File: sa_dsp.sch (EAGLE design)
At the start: 327 parts, among them CN1 uSD, CN3 2X5 HEADER, Q3 2N7002, Q4 2N7002, SW1 1825910-7, U1 PGA2311, U10 LME49720, U11 PGA2311, U12 LME49720, U13 LME49720, U14 PCM1754, U15 LME49720, U16 PGA2311, U17 LME49720, U18 LME49720, U19 PCM1754, U2 LM317, U20 LME49720, U21 7 SEG, U22 74HC164A, U23 PCM2707, U24 PCM2707, U25 7 SEG, U26 74HC164A, U27 LM337, U28 LM317, U29 7 SEG, U3 OSD3358-512M-BSM, U30 74HC164A, U31 100MHz, U4 LME49720, U5 LME49720, U6 10CL016YF484C6G, U7 7 SEG, U8 74HC164A, U9 PCM1754

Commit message: DSP progress
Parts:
- added C133: 2.2uF 25V, CAPACITORS:GRM188R61E225KA12D
- added C134, C138: 100pF 50V, CAPACITORS:C0603C101K5GACTU
- added C135, C136, C137, C139: 100nF 16V, CAPACITORS:CL10B104KO8WPNC
- added CN2, CN4: MINI B USB, CONNECTORs:MUSB-05-S-B-SM-A
- added FB17, FB6: 600R, INDUCTORS:742792651
- added TP3, TP4, TP5, TP6, TP7: 2MM_TEST_POINT, MISC:2MM_TEST_POINT
- added U32, U34: USBLC6-2SC6, ICs:USBLC6-2SC6
- added U33: FT230X, ICs:FT230XS
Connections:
- removed net AM_STM_NRST: U3C.GPMC_AD9
- removed net STM32_BOOT0: U3C.GPMC_AD10
- new net AM_I2C0_SCL: TP3.P$1, U3A.I2C0_SCL, U3A.PMIC_SCL
- new net AM_I2C0_SDA: TP4.P$1, U3A.I2C0_SDA, U3A.PMIC_SDA
- new net FT_DB_3V3: C133.2, C137.2, U33.!CTS, U33.!RESET, U33.3V3OUT, U33.VCCIO
- new net FT_DB_USB_5V: C134.2, C135.2, C136.2, FB6.2, U32.VBUS, U33.VCC
- new net N$183: CN2.D-, U32.D+_OUT
- new net N$199: CN2.D+, U32.D-OUT
- new net N$200: U32.D+_IN, U33.D-
- new net N$201: U32.D-_IN, U33.D+
- new net N$202: CN2.5V, FB6.1
- new net N$203: CN4.5V, FB17.1
- new net OSD_SPI_CS_FPGA: U3C.SPI0_CS0
- new net OSD_SPI_MISO: U3C.SPI0_D1
- new net OSD_SPI_MOSI: U3C.SPI0_D0
- new net OSD_SPI_SCLK: U3C.SPI0_SCLK
- net 5VUSB: now also C138.2, C139.2, FB17.2, U34.VBUS
- net AM_DEBUG_UART_RX: now also U33.RXD
- net AM_DEBUG_UART_TX: now also U33.TXD
- net AM_EEPROM_WP: now also TP5.P$1
- net AM_WARM_!RST: now also TP7.P$1
- net GND: now also C133.1, C134.1, C135.1, C136.1, C137.1, C138.1, C139.1, CN2.GND, CN4.GND, TP6.P$1, U32.GND, U33.GND, U34.GND
- net N$134: now also CN4.D-, U34.D-OUT; no longer U3A.I2C0_SCL, U3A.PMIC_SCL
- net N$135: now also CN4.D+, U34.D+_OUT; no longer U3A.I2C0_SDA, U3A.PMIC_SDA
- net N$172: now also R103.1, U34.D-_IN; no longer R102.1
- net N$173: now also R102.1, U34.D+_IN; no longer R103.1
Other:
- moved on the sheet: C119, C120, C121, C122, C123, C124, C125, C93, C94, C95, R102, R103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

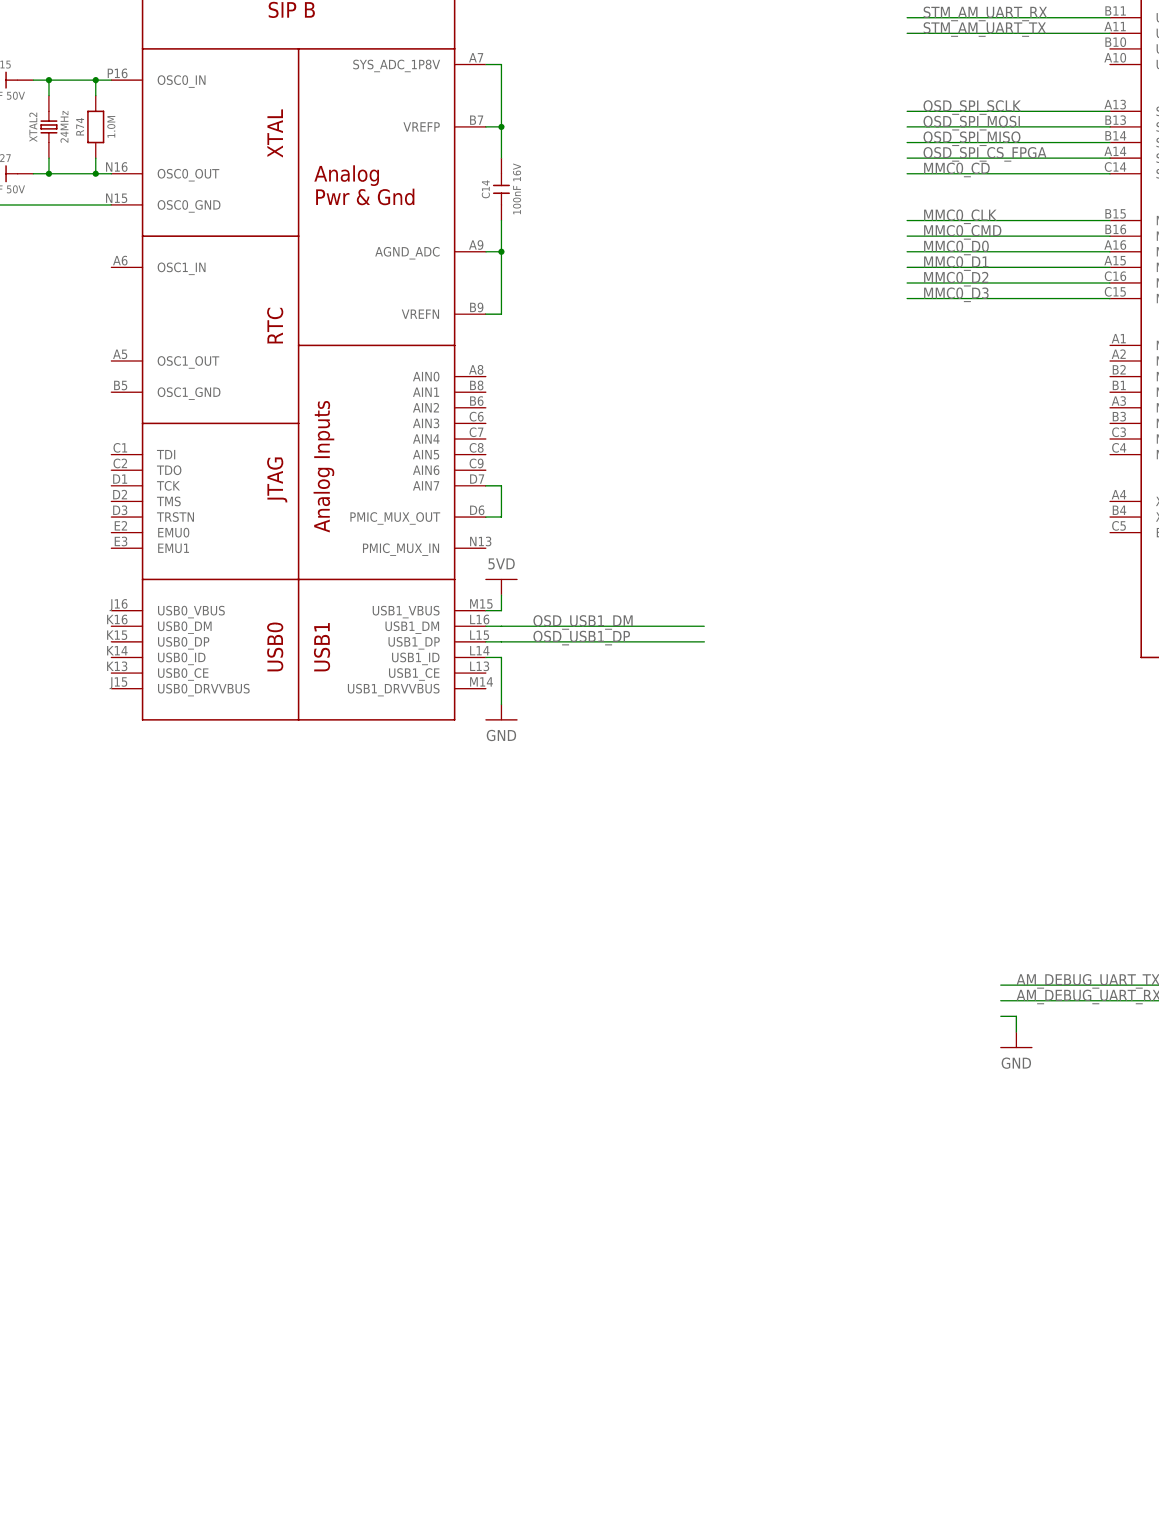
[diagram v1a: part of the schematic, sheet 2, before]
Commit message: Added female USB
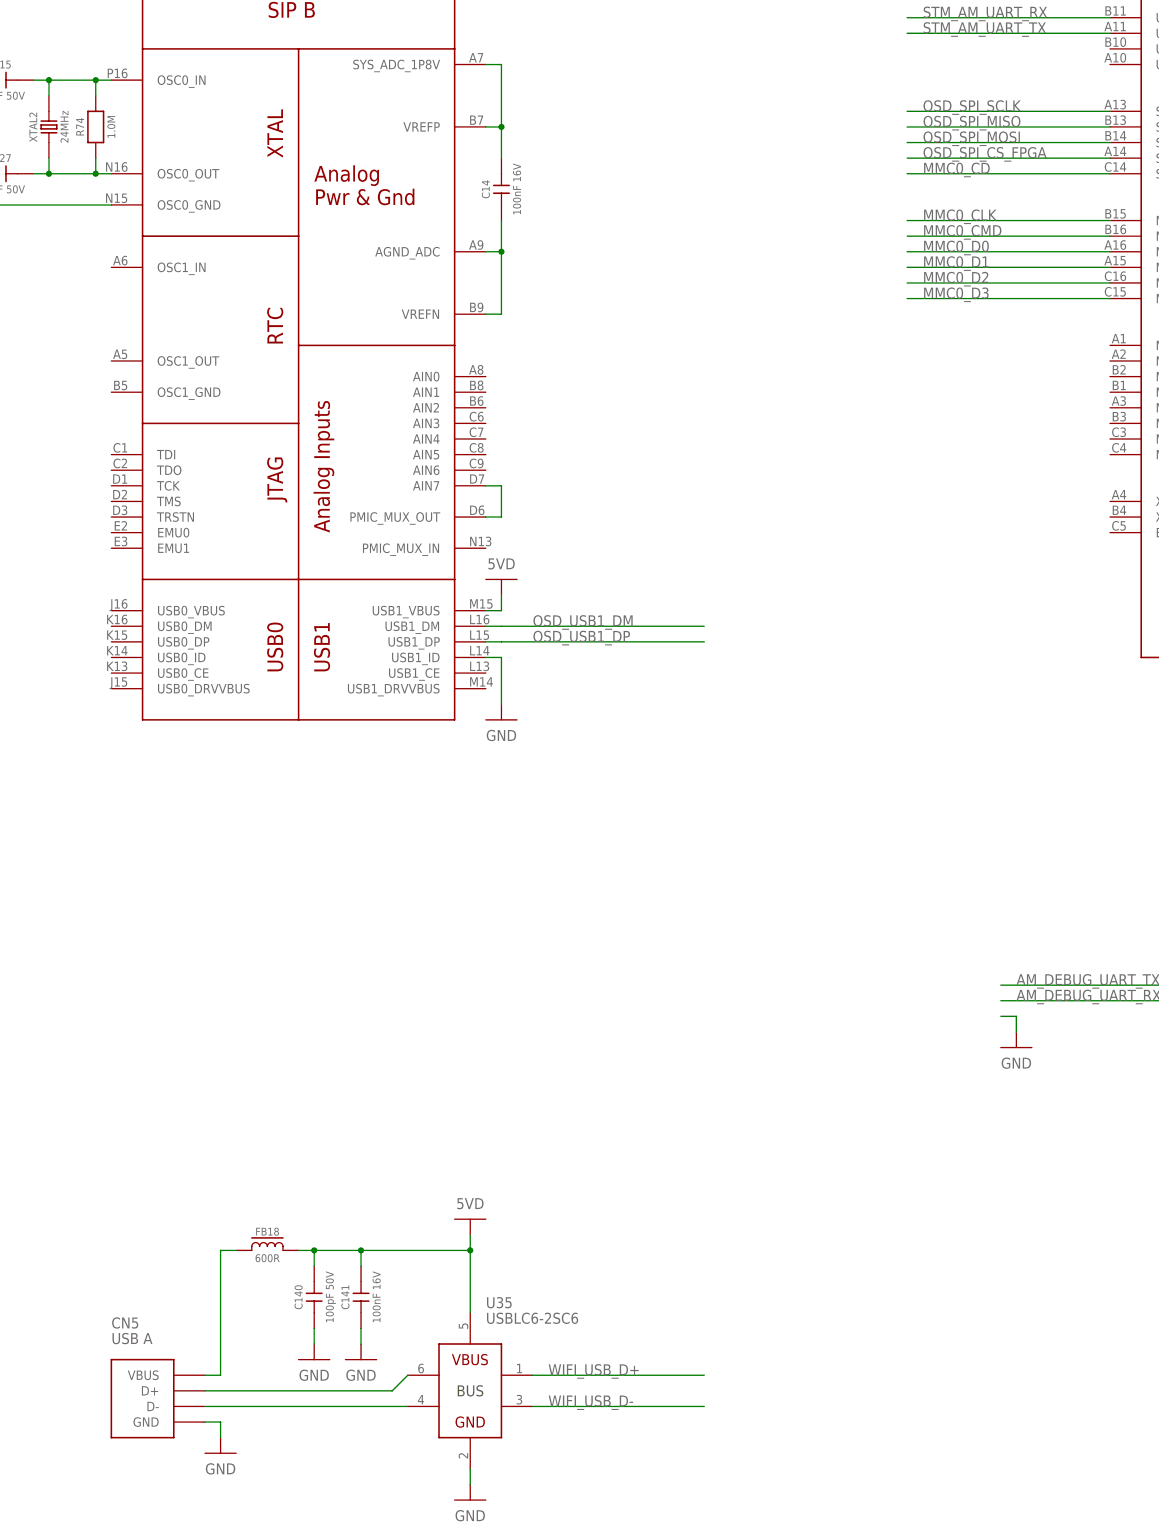
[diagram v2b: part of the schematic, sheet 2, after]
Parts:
- added C140: 100pF 50V, CAPACITORS:C0603C101K5GACTU
- added C141: 100nF 16V, CAPACITORS:CL10B104KO8WPNC
- added CN5: USB A, CONNECTORs:629104190121
- added FB18: 600R, INDUCTORS:742792651
- added U35: USBLC6-2SC6, ICs:USBLC6-2SC6
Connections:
- new net N$204: CN5.D-, U35.D-OUT
- new net N$205: CN5.D+, U35.D+_OUT
- new net N$206: CN5.VBUS, FB18.1
- new net WIFI_USB_D+: U35.D+_IN
- new net WIFI_USB_D-: U35.D-_IN
- net 5VD: now also C140.2, C141.2, FB18.2, U35.VBUS
- net GND: now also C140.1, C141.1, CN5.GND, U35.GND
- net OSD_SPI_MISO: now also U3C.SPI0_D0; no longer U3C.SPI0_D1
- net OSD_SPI_MOSI: now also U3C.SPI0_D1; no longer U3C.SPI0_D0
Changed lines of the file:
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@@
 <part name="U$200" library="NETS" deviceset="5VUSB" device=""/>
 <part name="TP7" library="MISC" deviceset="2MM_TEST_POINT" device=""/>
+<part name="CN5" library="CONNECTORs" deviceset="629104190121" device="" value="USB A"/>
+<part name="U$201" library="NETS" deviceset="5VD" device=""/>
+<part name="U35" library="ICs" deviceset="USBLC6-2SC6" device="" value="USBLC6-2SC6"/>
+<part name="GND130" library="NETS" deviceset="GND" device=""/>
+<part name="FB18" library="INDUCTORS" deviceset="742792651" device="" value="600R"/>
+<part name="C140" library="CAPACITORS" deviceset="C0603C101K5GACTU" device="" value="100pF 50V"/>
+<part name="C141" library="CAPACITORS" deviceset="CL10B104KO8WPNC" device="" value="100nF 16V"/>
+<part name="GND131" library="NETS" deviceset="GND" device=""/>
+<part name="GND132" library="NETS" deviceset="GND" device=""/>
+<part name="GND133" library="NETS" deviceset="GND" device=""/>
 </parts>
 <sheets>
@@
 <attribute name="NAME" x="-68.58" y="132.08" size="1.27" layer="97" rot="R90" align="center"/>
 </instance>
+<instance part="CN5" gate="G$1" x="205.74" y="-2.54" smashed="yes">
+<attribute name="NAME" x="200.66" y="7.62" size="1.778" layer="95"/>
+<attribute name="VALUE" x="200.66" y="5.08" size="1.778" layer="96"/>
+</instance>
+<instance part="U$201" gate="G$1" x="259.08" y="25.4" smashed="yes">
+<attribute name="VALUE" x="259.08" y="27.94" size="1.778" layer="96" rot="R180" align="center"/>
+</instance>
+<instance part="U35" gate="G$1" x="259.08" y="-2.54" smashed="yes" rot="MR0">
+<attribute name="NAME" x="261.62" y="12.7" size="1.778" layer="95" rot="MR180"/>
+<attribute name="VALUE" x="261.62" y="10.16" size="1.778" layer="95" rot="MR180"/>
+</instance>
+<instance part="GND130" gate="G$1" x="259.08" y="-20.32" smashed="yes">
+<attribute name="VALUE" x="259.08" y="-22.86" size="1.778" layer="96" align="center"/>
+</instance>
+<instance part="FB18" gate="G$1" x="226.06" y="20.32" smashed="yes">
+<attribute name="NAME" x="226.06" y="23.368" size="1.27" layer="95" align="center"/>
+<attribute name="VALUE" x="226.06" y="19.05" size="1.27" layer="96" align="center"/>
+</instance>
+<instance part="C140" gate="G$1" x="233.68" y="12.7" smashed="yes" rot="R90">
+<attribute name="NAME" x="231.14" y="12.7" size="1.27" layer="95" rot="R90" align="center"/>
+<attribute name="VALUE" x="236.22" y="12.7" size="1.27" layer="96" rot="R90" align="center"/>
+</instance>
+<instance part="C141" gate="G$1" x="241.3" y="12.7" smashed="yes" rot="R90">
+<attribute name="NAME" x="238.76" y="12.7" size="1.27" layer="95" rot="R90" align="center"/>
+<attribute name="VALUE" x="243.84" y="12.7" size="1.27" layer="96" rot="R90" align="center"/>
+</instance>
+<instance part="GND131" gate="G$1" x="241.3" y="2.54" smashed="yes">
+<attribute name="VALUE" x="241.3" y="0" size="1.778" layer="96" align="center"/>
+</instance>
+<instance part="GND132" gate="G$1" x="233.68" y="2.54" smashed="yes">
+<attribute name="VALUE" x="233.68" y="0" size="1.778" layer="96" align="center"/>
+</instance>
+<instance part="GND133" gate="G$1" x="218.44" y="-12.7" smashed="yes">
+<attribute name="VALUE" x="218.44" y="-15.24" size="1.778" layer="96" align="center"/>
+</instance>
 </instances>
 <busses>
@@
 <wire x1="523.24" y1="490.22" x2="523.24" y2="487.68" width="0.1524" layer="91"/>
 </segment>
+<segment>
+<pinref part="U35" gate="G$1" pin="GND"/>
+<pinref part="GND130" gate="G$1" pin="GND"/>
+<wire x1="259.08" y1="-17.78" x2="259.08" y2="-15.24" width="0.1524" layer="91"/>
+</segment>
+<segment>
+<pinref part="C141" gate="G$1" pin="1"/>
+<pinref part="GND131" gate="G$1" pin="GND"/>
+<wire x1="241.3" y1="7.62" x2="241.3" y2="5.08" width="0.1524" layer="91"/>
+</segment>
+<segment>
+<pinref part="C140" gate="G$1" pin="1"/>
+<pinref part="GND132" gate="G$1" pin="GND"/>
+<wire x1="233.68" y1="7.62" x2="233.68" y2="5.08" width="0.1524" layer="91"/>
+</segment>
+<segment>
+<pinref part="CN5" gate="G$1" pin="GND"/>
+<wire x1="215.9" y1="-7.62" x2="218.44" y2="-7.62" width="0.1524" layer="91"/>
+<pinref part="GND133" gate="G$1" pin="GND"/>
+<wire x1="218.44" y1="-7.62" x2="218.44" y2="-10.16" width="0.1524" layer="91"/>
+</segment>
 </net>
 <net name="N$124" class="0">
@@
 <label x="370.84" y="449.58" size="1.778" layer="95"/>
 </segment>
+<segment>
+<pinref part="U35" gate="G$1" pin="VBUS"/>
+<wire x1="259.08" y1="10.16" x2="259.08" y2="20.32" width="0.1524" layer="91"/>
+<wire x1="231.14" y1="20.32" x2="233.68" y2="20.32" width="0.1524" layer="91"/>
+<pinref part="FB18" gate="G$1" pin="2"/>
+<pinref part="C140" gate="G$1" pin="2"/>
+<wire x1="233.68" y1="20.32" x2="241.3" y2="20.32" width="0.1524" layer="91"/>
+<wire x1="241.3" y1="20.32" x2="259.08" y2="20.32" width="0.1524" layer="91"/>
+<wire x1="233.68" y1="17.78" x2="233.68" y2="20.32" width="0.1524" layer="91"/>
+<junction x="233.68" y="20.32"/>
+<pinref part="C141" gate="G$1" pin="2"/>
+<wire x1="241.3" y1="17.78" x2="241.3" y2="20.32" width="0.1524" layer="91"/>
+<junction x="241.3" y="20.32"/>
+<pinref part="U$201" gate="G$1" pin="5VD"/>
+<wire x1="259.08" y1="22.86" x2="259.08" y2="20.32" width="0.1524" layer="91"/>
+<junction x="259.08" y="20.32"/>
+</segment>
 </net>
 <net name="N$183" class="0">
@@
 </segment>
 </net>
-<net name="OSD_SPI_MOSI" class="0">
+<net name="OSD_SPI_MISO" class="0">
 <segment>
 <pinref part="U3" gate="C" pin="SPI0_D0"/>
@@
 </segment>
 </net>
-<net name="OSD_SPI_MISO" class="0">
+<net name="OSD_SPI_MOSI" class="0">
 <segment>
 <pinref part="U3" gate="C" pin="SPI0_D1"/>
@@
 </segment>
 </net>
+<net name="N$204" class="0">
+<segment>
+<pinref part="U35" gate="G$1" pin="D-OUT"/>
+<pinref part="CN5" gate="G$1" pin="D-"/>
+<wire x1="248.92" y1="-5.08" x2="215.9" y2="-5.08" width="0.1524" layer="91"/>
+</segment>
+</net>
+<net name="N$205" class="0">
+<segment>
+<pinref part="CN5" gate="G$1" pin="D+"/>
+<pinref part="U35" gate="G$1" pin="D+_OUT"/>
+<wire x1="215.9" y1="-2.54" x2="246.38" y2="-2.54" width="0.1524" layer="91"/>
+<wire x1="246.38" y1="-2.54" x2="248.92" y2="0" width="0.1524" layer="91"/>
+</segment>
+</net>
+<net name="N$206" class="0">
+<segment>
+<pinref part="FB18" gate="G$1" pin="1"/>
+<wire x1="220.98" y1="20.32" x2="218.44" y2="20.32" width="0.1524" layer="91"/>
+<wire x1="218.44" y1="20.32" x2="218.44" y2="0" width="0.1524" layer="91"/>
+<pinref part="CN5" gate="G$1" pin="VBUS"/>
+<wire x1="218.44" y1="0" x2="215.9" y2="0" width="0.1524" layer="91"/>
+</segment>
+</net>
+<net name="WIFI_USB_D+" class="0">
+<segment>
+<pinref part="U35" gate="G$1" pin="D+_IN"/>
+<wire x1="269.24" y1="0" x2="297.18" y2="0" width="0.1524" layer="91"/>
+<label x="271.78" y="0" size="1.778" layer="95"/>
+</segment>
+</net>
+<net name="WIFI_USB_D-" class="0">
+<segment>
+<pinref part="U35" gate="G$1" pin="D-_IN"/>
+<wire x1="269.24" y1="-5.08" x2="297.18" y2="-5.08" width="0.1524" layer="91"/>
+<label x="271.78" y="-5.08" size="1.778" layer="95"/>
+</segment>
+</net>

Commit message: USB hub added
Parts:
- added C149, C150: 10pF 100V, CAPACITORS:06031A100FAT2A
- added C151, C152, C153, C154, C155: 100nF 16V, CAPACITORS:CL10B104KO8WPNC
- added CN6: MINI B USB, CONNECTORs:MUSB-05-S-B-SM-A
- added R133: 10k, r_0603:ERJ3EKF1002V
- added R134: 20k, r_0603:ERJ3EKF2002V
- added R135, R137, R138: 51k, r_0603:ERJ3EKF5102V
- added R136: 12k, r_0603:ERJ3EKF1202V
- added R139: 1.0M, r_0603:ERJ3EKF1004V
- added U36: USBLC6-2SC6, ICs:USBLC6-2SC6
- added U37: 2 PORT HUB, ICs:USB2412
- added XTAL5: 24MHz, CRYSTALS:7A-24.000MAAJ-T
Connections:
- removed net WIFI_USB_D+: U35.D+_IN
- removed net WIFI_USB_D-: U35.D-_IN
- new net N$207: U3B.USB1_DRVVBUS, U3B.USB1_VBUS
- new net N$208: CN6.D+, U36.D+_OUT
- new net N$209: CN6.D-, U36.D-OUT
- new net N$229: R133.2, R134.2, U37.VBUS_DECT
- new net N$230: R135.2, U37.HS_IND
- new net N$231: R136.2, U37.RBIAS
- new net N$232: R138.2, U37.NON_REM1
- new net N$233: R137.2, U37.SUSP_IND/NON_REM0
- new net N$234: C150.2, R139.2, U37.XTALIN/CLKLIN, XTAL5.P$1
- new net N$235: C149.2, R139.1, U37.XTALOUT, XTAL5.P$2
- new net OSD_DEBUG_USB_DM: U36.D-_IN, U3B.USB0_DM
- new net OSD_DEBUG_USB_DP: U36.D+_IN, U3B.USB0_DP
- new net OSD_DEBUG_USB_ID: CN6.ID, U3B.USB0_ID
- new net USB_OUT0_DN: U35.D-_IN, U37.USB_DN1_DN
- new net USB_OUT0_DP: U35.D+_IN, U37.USB_DN1_DP
- new net USB_OUT1_DN: R89.1, U37.USB_DN2_DN
- new net USB_OUT1_DP: R88.1, U37.USB_DN2_DP
- new net USB_RESET: U37.!RESET
- net 3V3: now also C151.2, C152.2, C153.2, C154.2, C155.2, U37.VDD
- net 5VD: now also U3B.USB0_VBUS; no longer U3B.USB1_VBUS
- net 5VUSB: now also R133.1
- net GND: now also C149.1, C150.1, C151.1, C152.1, C153.1, C154.1, C155.1, CN6.GND, R134.1, R135.1, R136.1, R137.1, R138.1, U36.GND, U37.GND
- net OSD_USB1_DM: now also U37.USB_UP_DN; no longer R89.1
- net OSD_USB1_DP: now also U37.USB_UP_DP; no longer R88.1
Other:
- moved on the sheet: C140, C141, CN5, FB18, U35

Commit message: Working on PSUs
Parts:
- added C142, C157: 47uF 25V, CAPACITORS:C3216X5R1E476M160AC
- added C147: 10nF 50V, CAPACITORS:CL10B103KB8NCNC
- added C148: 47uF 10V, CAPACITORS:GRM31CR61A476ME15L
- added C156: 100nF 16V, CAPACITORS:CL10B104KO8WPNC
- added C158: 100nF 100V, CAPACITORS:06031C104KAT2A
- added D8: BC560, DIODES:BC560C
- added L5: 47uH 3.1A, INDUCTORS:SRR1210-470M
- added R128: 160k, r_0603:ERJ3EKF1603V
- added U39: LM22670, ICs:LM22670MRX-5.0/NOPB
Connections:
- removed net N$207: U3B.USB1_DRVVBUS, U3B.USB1_VBUS
- new net N$212: C147.1, U39.BOOT
- new net N$213: C147.2, D8.K, L5.1, U39.SW
- new net N$236: R128.2, U39.RT_SYNC
- new net OSD_USB1_VBUS: R133.1, U3B.USB1_DRVVBUS, U3B.USB1_VBUS
- net 15VD_UNREG: now also C142.1, C157.1, C158.2, U39.VIN
- net 5V: now also C148.2, C156.2, L5.2, U39.FB
- net 5VUSB: no longer R133.1
- net GND: now also C142.2, C148.1, C156.1, C157.2, C158.1, D8.A, R128.1, U39.GND
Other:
- moved on the sheet: R133

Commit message: Progress on DSP
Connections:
- removed net STM_AM_UART_RX: U3C.UART1_TXD
- removed net STM_AM_UART_TX: U3C.UART1_RXD
- new net OSD_FPGA_GPIO0: U3C.GPMC_A0, U6.B1_IO14
- new net OSD_FPGA_GPIO1: U3C.GPMC_A1, U6.B1_IO12
- new net OSD_FPGA_GPIO2: U3C.GPMC_A2, U6.B1_IO11
- new net OSD_FPGA_GPIO3: U3C.GPMC_A3, U6.B2_IO5
- new net OSD_FPGA_GPIO4: U3C.GPMC_A4, U6.B1_IO13
- new net OSD_FPGA_GPIO5: U3C.GPMC_A9, U6.B2_IO9
- new net OSD_FPGA_GPIO6: U3C.GPMC_A10, U6.B2_IO4
- new net OSD_FPGA_GPIO7: U3C.GPMC_A11, U6.B2_IO8
- net 5V: no longer C148.2, C156.2, L5.2, U39.FB
- net 5VD: now also C148.2, C156.2, L5.2, U39.FB
- net OSD_SPI_CS_FPGA: now also U6.B1_IO2
- net OSD_SPI_MISO: now also U6.B1_IO6
- net OSD_SPI_MOSI: now also U6.B1_IO7
- net OSD_SPI_SCLK: now also U6.B1_IO1
- net PCM_I2S_BCLK_BB: now also U6.B1_CLK0
- net PCM_I2S_BCLK_EXT: now also U6.B2_IO28
- net PCM_I2S_DOUT_BB: now also U6.B1_IO24
- net PCM_I2S_DOUT_EXT: now also U6.B2_IO29
- net PCM_I2S_LRCLK_BB: now also U6.B1_IO23
- net PCM_I2S_LRCLK_EXT: now also U6.B2_IO31
- net PCM_I2S_MCLK_BB: now also U6.B1_CLK1
- net PCM_I2S_MCLK_EXT: now also U6.B2_CLK2
